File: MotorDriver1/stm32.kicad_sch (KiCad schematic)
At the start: 12 parts, among them IC1 STM32C092RCT6, SW1 KSC321JLFS, Y1 32.768 kHz, Y2 48 MHz

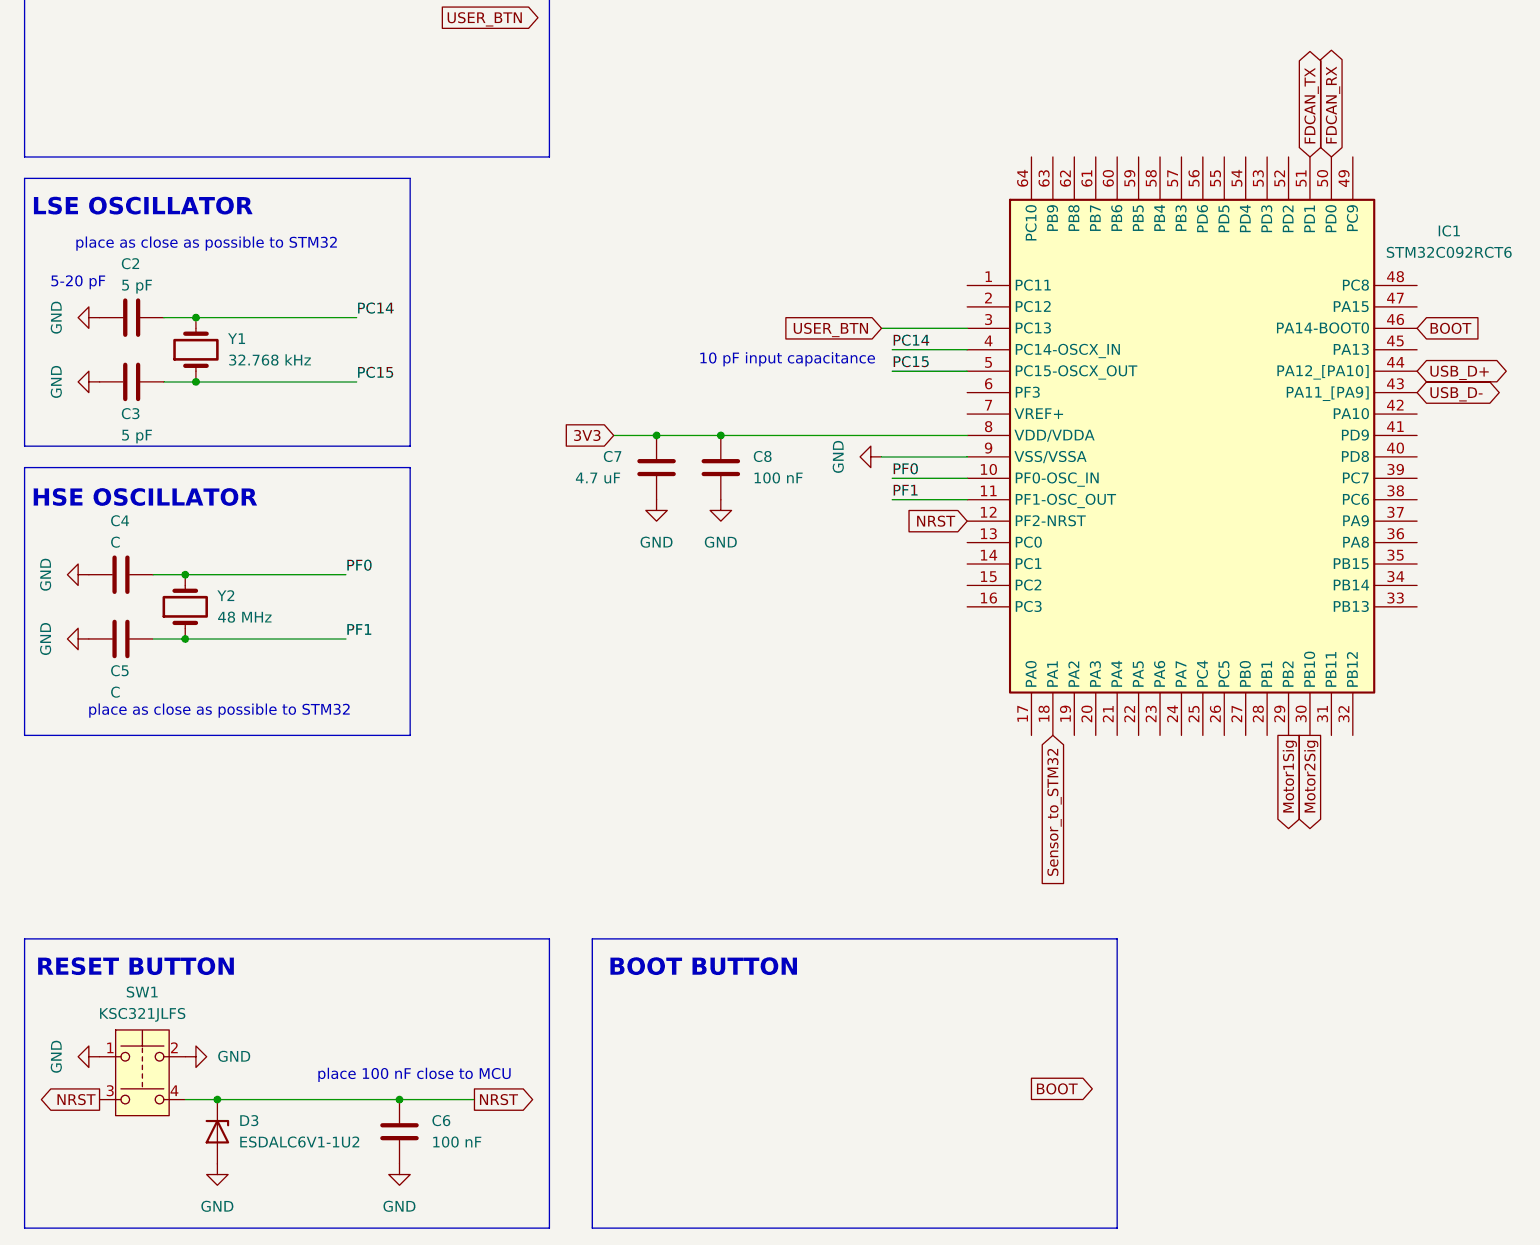
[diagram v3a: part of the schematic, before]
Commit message: updated motor and sensor schematics and added footprints
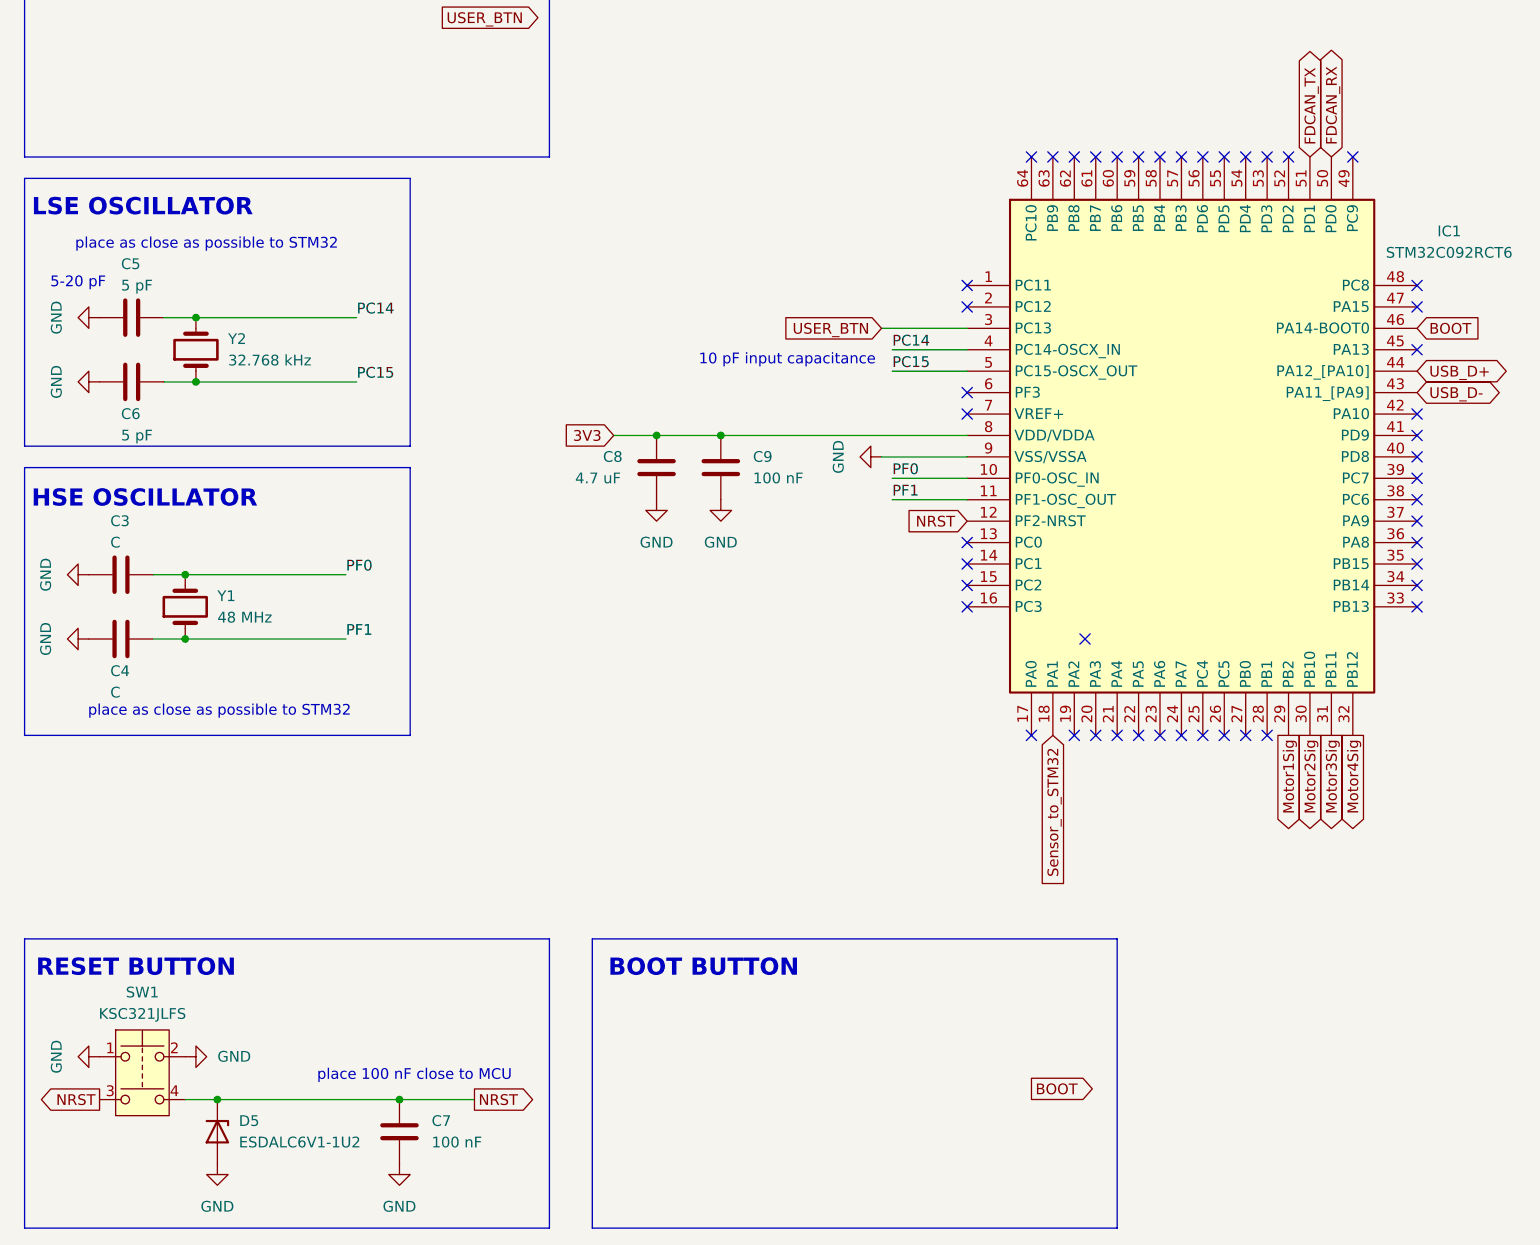
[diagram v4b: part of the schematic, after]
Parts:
- IC1: footprint QFP50P1200X1200X160-64N -> (none)
- renumbered C4 to C3, C5 to C4, C2 to C5, C3 to C6, C6 to C7, C7 to C8, C8 to C9, D3 to D5, Y2 to Y1, Y1 to Y2
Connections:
- net Motor3Sig: now reaches IC1.31 (PB11)
- net Motor4Sig: now reaches IC1.32 (PB12)
- no-connect marks 0 -> 47

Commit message: missing crystal verification
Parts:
- added C10: 10 nF, symbol Device:C
- added C11, C14: 100nF, symbol Device:C
- added C15: 10uF, symbol Device:C
- added C3: 6 pF, symbol Device:C
- added D5, D6: ESDALC6V1-1U2, symbol Device:D_Zener
- added IC3: TPS22916CNYFPR, BGA4C40P2X2_78X78X50, symbol pcb:TPS22916CNYFPR
- added J2: GT-USB-7010ASV, footprintLib:USB4110-GF-A_GCT, symbol pcb:USB4110-GF-A
- added R10, R9: 10k, symbol Device:R
- added R11, R12: 5.1k,10%, symbol Device:R
- added R13: DNP, symbol Device:R
- added R18, R19: 10k, 1%, symbol Device:R
- added SW1, SW3: K2-6639SP-C4SC-04, symbol Switch:SW_Push_Dual
- added U1: CH340X, Package_SO:MSOP-10_3x3mm_P0.5mm, symbol Interface_USB:CH340X
- C4: value C -> 6 pF
- C?: renamed from C3; value C -> 100nF
- SW2: renamed from SW1; value KSC321JLFS -> K2-6639SP-C4SC-04
- renumbered D5 to D?
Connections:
- net 3V3: now also SW2.1, SW2.2, C11.2, R10.1, U1.7 (VCC)
- net BOOT: now also D?.1 (K), SW2.3, SW2.4, R13.2, R9.1
- net GND: now also C10.2, C11.1, C14.1, C15.1, C3.1, D5.2 (A), D6.2 (A), IC3.B1 (GND), J2.15 (GND), J2.16 (GND), J2.17 (GND), J2.18 (GND), J2.A1-B12 (GND), J2.A12-B1 (GND), R11.1, R12.1, R18.2, R9.2, SW1.1, SW1.2, U1.3 (GND); no longer SW2.1, SW2.2
- net NRST: now also D5.1 (K), SW1.3, SW1.4; no longer D?.1 (K), SW2.3, SW2.4
- net PF0: now also C3.2; no longer C?.2
- net Sensor_to_STM32: now also IC1.28 (PB1); no longer IC1.18 (PA1)
- net USB_D+: now also J2.A6 (DP1), J2.B6 (DP2), U1.1 (UD+); no longer IC1.44 (PA12_[PA10])
- net USB_D-: now also J2.A7 (DN1), J2.B7 (DN2), U1.2 (UD-); no longer IC1.43 (PA11_[PA9])
- net USER_BTN: now also D6.1 (K), SW3.3, SW3.4
- net !CTS: now reaches IC1.17 (PA0)
- net !CTS: now also U1.5 (~{CTS})
- net USART2_TX: now reaches IC1.19 (PA2)
- net USART2_TX: now also U1.9 (RXD)
- net USART2_RX: now reaches IC1.20 (PA3)
- net USART2_RX: now also U1.8 (TXD)
- net FDCAN_STBY_STM: now reaches IC1.52 (PD2)
- net FDCAN_RX renamed FDCAN_RX_STM
- net FDCAN_TX renamed FDCAN_TX_STM
- new net: J2.A5 (CC1), R11.2
- new net: IC3.B2 (ON), R18.1, R19.1
- new net: R10.2, SW3.1, SW3.2
- new net: C10.1, U1.10 (V3)
- new net: J2.B5 (CC2), R12.2
- new net !DTR: R13.1, U1.6 (TNOW/~{DTR})
- new net !RTS: IC1.18 (PA1), U1.4 (~{RTS})
- new net 5V_USB: C14.2, C15.2, IC3.A1 (VOUT)
- new net VBUS: C?.2, IC3.A2 (VIN), J2.A4-B9 (VBUS), J2.A9-B4 (VBUS), R19.2
- no-connect marks 47 -> 46
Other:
- note added: "Keep nearby VCC"
- note added: "STM32C092RCT6 has internal flash"
- note added: "clear to send"
- note added: "could be possible that we don't need to hold boot with !DTR"
- note added: "data terminal ready"
- note added: "request to send"
- note removed: "BOOT BUTTON"
- note removed: "HSE OSCILLATOR"
- note removed: "LSE OSCILLATOR"
- note removed: "RESET BUTTON"
- note removed: "USER BUTTON"
- moved on the sheet: C4, C8, C9, C?, D?, IC1, SW2, Y1

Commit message: Updated footprints
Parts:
- gave numbers to parts that had none: 2
- renumbered C15 to C10, C14 to C12, C10 to C13, IC3 to IC2, J2 to J1, R13 to R10, R9 to R11, R11 to R12, R18 to R13, R19 to R14, R12 to R15, R10 to R9, SW3 to SW1, SW1 to SW2, SW2 to SW3
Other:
- moved on the sheet: R12

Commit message: assigned eo footprints
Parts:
- C10: footprint (none) -> Capacitor_SMD:C_1206_3216Metric
- C11, C12, C14, C7, C9: footprint (none) -> Capacitor_SMD:C_0402_1005Metric
- C13, C3, C4, C5, C6: footprint (none) -> Capacitor_SMD:C_0201_0603Metric
- C8: footprint (none) -> Capacitor_SMD:C_0603_1608Metric
- D5, D6, D7: footprint (none) -> Diode_SMD:D_0201_0603Metric
- IC1: footprint (none) -> footprintLib:QFP50P1200X1200X160-64N
- IC2: footprint BGA4C40P2X2_78X78X50 -> footprintLib:BGA6N40P3X2_157X88X50N
- R10, R11, R12, R13, R14, R15, R9: footprint (none) -> Resistor_SMD:R_0402_1005Metric
- SW1, SW2, SW3: footprint (none) -> Button_Switch_SMD:SW_Push_1P1T_NO_CK_KSC6xxJ
- Y1, Y2: footprint (none) -> footprintLib:XTAL_ECS-.327-12.5-12R-TR
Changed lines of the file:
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@@
 			)
 		)
-		(property "Footprint" ""
+		(property "Footprint" "Diode_SMD:D_0201_0603Metric"
 			(at 111.76 181.61 0)
 			(effects
@@
 			)
 		)
-		(property "Footprint" ""
+		(property "Footprint" "Diode_SMD:D_0201_0603Metric"
 			(at 38.1 180.34 0)
 			(effects
@@
 			)
 		)
-		(property "Footprint" ""
+		(property "Footprint" "Resistor_SMD:R_0402_1005Metric"
 			(at 193.04 36.068 90)
 			(effects
@@
 			)
 		)
-		(property "Footprint" ""
+		(property "Footprint" "Capacitor_SMD:C_0402_1005Metric"
 			(at 60.6552 184.15 0)
 			(effects
@@
 			)
 		)
-		(property "Footprint" ""
+		(property "Footprint" "Button_Switch_SMD:SW_Push_1P1T_NO_CK_KSC6xxJ"
 			(at 100.33 167.64 0)
 			(effects
@@
 			)
 		)
-		(property "Footprint" ""
+		(property "Footprint" "Button_Switch_SMD:SW_Push_1P1T_NO_CK_KSC6xxJ"
 			(at 29.21 166.37 0)
 			(effects
@@
 			)
 		)
-		(property "Footprint" ""
+		(property "Footprint" "Capacitor_SMD:C_0603_1608Metric"
 			(at 81.5848 97.79 0)
 			(effects
@@
 			)
 		)
-		(property "Footprint" ""
+		(property "Footprint" "Capacitor_SMD:C_0201_0603Metric"
 			(at 24.13 92.4052 0)
 			(effects
@@
 			)
 		)
-		(property "Footprint" ""
+		(property "Footprint" "Resistor_SMD:R_0402_1005Metric"
 			(at 264.16 93.218 90)
 			(effects
@@
 			)
 		)
-		(property "Footprint" ""
+		(property "Footprint" "Resistor_SMD:R_0402_1005Metric"
 			(at 131.572 181.61 90)
 			(effects
@@
 			)
 		)
-		(property "Footprint" ""
+		(property "Footprint" "Capacitor_SMD:C_0201_0603Metric"
 			(at 22.86 125.4252 0)
 			(effects
@@
 			)
 		)
-		(property "Footprint" ""
+		(property "Footprint" "Button_Switch_SMD:SW_Push_1P1T_NO_CK_KSC6xxJ"
 			(at 27.94 40.64 0)
 			(effects
@@
 			)
 		)
-		(property "Footprint" ""
+		(property "Footprint" "Capacitor_SMD:C_1206_3216Metric"
 			(at 204.7748 88.9 0)
 			(effects
@@
 			)
 		)
-		(property "Footprint" ""
+		(property "Footprint" "Capacitor_SMD:C_0402_1005Metric"
 			(at 91.1352 105.41 0)
 			(effects
@@
 			)
 		)
-		(property "Footprint" ""
+		(property "Footprint" "Capacitor_SMD:C_0402_1005Metric"
 			(at 209.8548 144.78 0)
 			(effects
@@
 			)
 		)
-		(property "Footprint" ""
+		(property "Footprint" "Capacitor_SMD:C_0201_0603Metric"
 			(at 256.54 122.2248 0)
 			(effects
@@
 			)
 		)
-		(property "Footprint" ""
+		(property "Footprint" "Capacitor_SMD:C_0201_0603Metric"
 			(at 31.75 82.8548 0)
 			(effects
@@
 			)
 		)
-		(property "Footprint" ""
+		(property "Footprint" "Capacitor_SMD:C_0402_1005Metric"
 			(at 214.9348 88.9 0)
 			(effects
@@
 			)
 		)
-		(property "Footprint" ""
+		(property "Footprint" "Capacitor_SMD:C_0402_1005Metric"
 			(at 254.3048 41.91 0)
 			(effects
@@
 			)
 		)
-		(property "Footprint" ""
+		(property "Footprint" "Capacitor_SMD:C_0201_0603Metric"
 			(at 30.48 115.8748 0)
 			(effects
@@
 			)
 		)
-		(property "Footprint" ""
+		(property "Footprint" "Resistor_SMD:R_0402_1005Metric"
 			(at 271.78 35.052 90)
 			(effects
@@
 			)
 		)
-		(property "Footprint" ""
+		(property "Footprint" "footprintLib:QFP50P1200X1200X160-64N"
 			(at 168.91 167.31 0)
 			(effects
@@
 			)
 		)
-		(property "Footprint" ""
+		(property "Footprint" "Resistor_SMD:R_0402_1005Metric"
 			(at 42.672 41.91 90)
 			(effects
@@
 			)
 		)
-		(property "Footprint" ""
+		(property "Footprint" "footprintLib:XTAL_ECS-.327-12.5-12R-TR"
 			(at 34.29 120.65 0)
 			(effects
@@
 			)
 		)
-		(property "Footprint" ""
+		(property "Footprint" "Resistor_SMD:R_0402_1005Metric"
 			(at 256.032 97.79 90)
 			(effects
@@
 			)
 		)
-		(property "Footprint" "BGA4C40P2X2_78X78X50"
+		(property "Footprint" "footprintLib:BGA6N40P3X2_157X88X50N"
 			(at 254 183.82 0)
 			(effects
@@
 			)
 		)
-		(property "Footprint" ""
+		(property "Footprint" "footprintLib:XTAL_ECS-.327-12.5-12R-TR"
 			(at 35.56 87.63 0)
 			(effects
@@
 			)
 		)
-		(property "Footprint" ""
+		(property "Footprint" "Diode_SMD:D_0201_0603Metric"
 			(at 39.37 54.61 0)
 			(effects
@@
 			)
 		)
-		(property "Footprint" ""
+		(property "Footprint" "Resistor_SMD:R_0402_1005Metric"
 			(at 125.73 174.498 90)
 			(effects

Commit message: laid out PCB
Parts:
- removed C10: 10uF, Capacitor_SMD:C_1206_3216Metric, symbol Device:C
- removed C12: 100nF, Capacitor_SMD:C_0402_1005Metric, symbol Device:C
- removed IC2: TPS22916CNYFPR, footprintLib:BGA6N40P3X2_157X88X50N, symbol pcb:TPS22916CNYFPR
- added C13: 100nF, Capacitor_SMD:C_0402_1005Metric, symbol Device:C
- added C14: 10uF, Capacitor_SMD:C_1206_3216Metric, symbol Device:C
- added U1: TPS22916CNYFPR, footprintLib:TPS22916CNYFPR, symbol pcb:TPS22916CNYFPR
- SW1, SW2, SW3: footprint Button_Switch_SMD:SW_Push_1P1T_NO_CK_KSC6xxJ -> footprintLib:K2-6639SP-C4SC-04
- renumbered C11 to C10, C13 to C11, C14 to C12, U1 to U2
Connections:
- net 5V_USB: now also C13.2, C14.2, U1.A1 (VOUT)
- net GND: now also R14.2, C13.1, C14.1, U1.B1 (GND); no longer R13.2
- net VBUS: now also R13.2, U1.A2 (VIN); no longer R14.2
- net at R13.1, R14.1: now also U1.B2 (ON)
- net SensorAOut: now reaches IC1.21 (PA4)
- net Motor4_PWM: now reaches IC1.24 (PA7)
- net SensorDOut: now reaches IC1.27 (PB0)
- net Motor1_PWM: now reaches IC1.47 (PA15)
- net Motor2_PWM: now reaches IC1.57 (PB3)
- net Motor3_PWM: now reaches IC1.58 (PB4)
- net Motor1Sig: no longer names the net of IC1.29 (PB2)
- net Motor2Sig: no longer names the net of IC1.30 (PB10)
- net Motor3Sig: no longer names the net of IC1.31 (PB11)
- net Motor4Sig: no longer names the net of IC1.32 (PB12)
- net Sensor_to_STM32: no longer names the net of IC1.28 (PB1)
- no-connect marks 46 -> 45
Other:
- moved on the sheet: R12
